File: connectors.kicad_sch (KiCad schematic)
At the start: 4 parts, among them J1 Conn_01x04_Pin, J2 Conn_01x04_Pin, J3 Conn_01x09_Pin, J4 Conn_02x03_Odd_Even

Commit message: Associated footprints
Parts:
- J1, J2: footprint (none) -> Connector_PinHeader_2.54mm:PinHeader_1x04_P2.54mm_Vertical
- J3: footprint (none) -> Connector_PinHeader_2.54mm:PinHeader_1x09_P2.54mm_Vertical
- J4: footprint (none) -> Connector_PinHeader_2.54mm:PinHeader_2x03_P2.54mm_Vertical
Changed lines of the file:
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@@
 			)
 		)
-		(property "Footprint" ""
+		(property "Footprint" "Connector_PinHeader_2.54mm:PinHeader_1x04_P2.54mm_Vertical"
 			(at 156.21 95.25 0)
 			(effects
@@
 			)
 		)
-		(property "Footprint" ""
+		(property "Footprint" "Connector_PinHeader_2.54mm:PinHeader_2x03_P2.54mm_Vertical"
 			(at 146.05 119.38 0)
 			(effects
@@
 			)
 		)
-		(property "Footprint" ""
+		(property "Footprint" "Connector_PinHeader_2.54mm:PinHeader_1x09_P2.54mm_Vertical"
 			(at 184.15 99.06 0)
 			(effects
@@
 			)
 		)
-		(property "Footprint" ""
+		(property "Footprint" "Connector_PinHeader_2.54mm:PinHeader_1x04_P2.54mm_Vertical"
 			(at 133.35 95.25 0)
 			(effects

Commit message: Wiring complete
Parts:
- J1, J2: footprint Connector_PinHeader_2.54mm:PinHeader_1x04_P2.54mm_Vertical -> (none)
- J3: footprint Connector_PinHeader_2.54mm:PinHeader_1x09_P2.54mm_Vertical -> (none)
- J4: footprint Connector_PinHeader_2.54mm:PinHeader_2x03_P2.54mm_Vertical -> (none)
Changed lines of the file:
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@@
 			)
 		)
-		(property "Footprint" "Connector_PinHeader_2.54mm:PinHeader_1x04_P2.54mm_Vertical"
+		(property "Footprint" ""
 			(at 156.21 95.25 0)
 			(effects
@@
 			)
 		)
-		(property "Footprint" "Connector_PinHeader_2.54mm:PinHeader_2x03_P2.54mm_Vertical"
+		(property "Footprint" ""
 			(at 146.05 119.38 0)
 			(effects
@@
 			)
 		)
-		(property "Footprint" "Connector_PinHeader_2.54mm:PinHeader_1x09_P2.54mm_Vertical"
+		(property "Footprint" ""
 			(at 184.15 99.06 0)
 			(effects
@@
 			)
 		)
-		(property "Footprint" "Connector_PinHeader_2.54mm:PinHeader_1x04_P2.54mm_Vertical"
+		(property "Footprint" ""
 			(at 133.35 95.25 0)
 			(effects

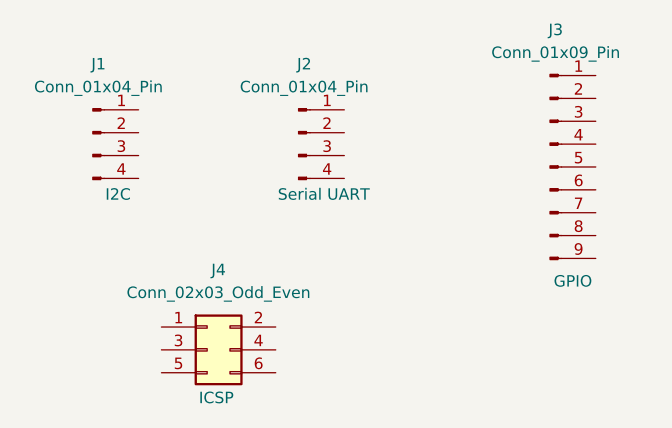
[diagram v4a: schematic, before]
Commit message: Allocated Vcc and GND nets to Power netclass
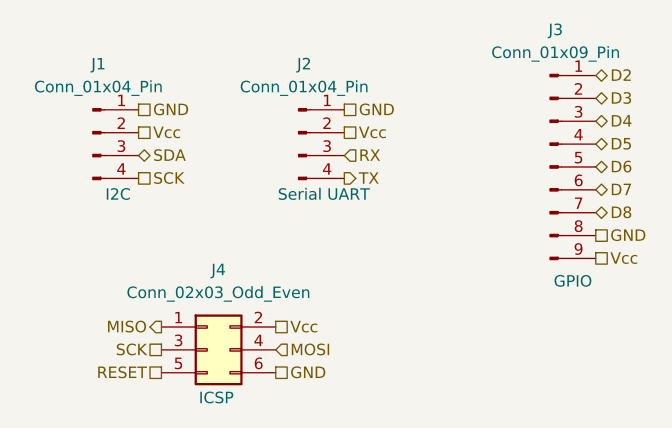
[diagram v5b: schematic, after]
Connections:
- net GND: now reaches J2.1 (Pin_1)
- net GND: now also J1.1 (Pin_1), J3.8 (Pin_8), J4.6 (Pin_6)
- net Vcc: now reaches J2.2 (Pin_2)
- net Vcc: now also J1.2 (Pin_2), J3.9 (Pin_9), J4.2 (Pin_2)
- net RX: now reaches J2.3 (Pin_3)
- net TX: now reaches J2.4 (Pin_4)
- net MISO: now reaches J4.1 (Pin_1)
- net SCK: now reaches J4.3 (Pin_3)
- net SCK: now also J1.4 (Pin_4)
- net MOSI: now reaches J4.4 (Pin_4)
- net RESET: now reaches J4.5 (Pin_5)
- net D2: now reaches J3.1 (Pin_1)
- net D3: now reaches J3.2 (Pin_2)
- net D4: now reaches J3.3 (Pin_3)
- net D5: now reaches J3.4 (Pin_4)
- net D6: now reaches J3.5 (Pin_5)
- net D7: now reaches J3.6 (Pin_6)
- net D8: now reaches J3.7 (Pin_7)
- net SDA: now reaches J1.3 (Pin_3)

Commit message: Placed footprints on layout
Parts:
- J1, J2: footprint (none) -> Connector_PinHeader_2.54mm:PinHeader_1x04_P2.54mm_Vertical
- J3: footprint (none) -> Connector_PinHeader_2.54mm:PinHeader_1x09_P2.54mm_Vertical
- J4: footprint (none) -> Connector_PinHeader_2.54mm:PinHeader_2x03_P2.54mm_Vertical
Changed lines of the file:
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@@
 			)
 		)
-		(property "Footprint" ""
+		(property "Footprint" "Connector_PinHeader_2.54mm:PinHeader_1x04_P2.54mm_Vertical"
 			(at 156.21 95.25 0)
 			(effects
@@
 			)
 		)
-		(property "Footprint" ""
+		(property "Footprint" "Connector_PinHeader_2.54mm:PinHeader_2x03_P2.54mm_Vertical"
 			(at 146.05 119.38 0)
 			(effects
@@
 			)
 		)
-		(property "Footprint" ""
+		(property "Footprint" "Connector_PinHeader_2.54mm:PinHeader_1x09_P2.54mm_Vertical"
 			(at 184.15 99.06 0)
 			(effects
@@
 			)
 		)
-		(property "Footprint" ""
+		(property "Footprint" "Connector_PinHeader_2.54mm:PinHeader_1x04_P2.54mm_Vertical"
 			(at 133.35 95.25 0)
 			(effects
